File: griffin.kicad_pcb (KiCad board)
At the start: 2 copper layers, 150 x 100 mm, 41 parts, among them IC1 ME6211C33M5G-N, J1 USB_B_Micro, J2 Conn_02x03_Odd_Even, J3 Conn_01x04, J4 Conn_01x11, J5 Conn_01x04, J6 Conn_01x20, J7 Conn_01x20, J8 Conn_01x14, J9 Conn_01x08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

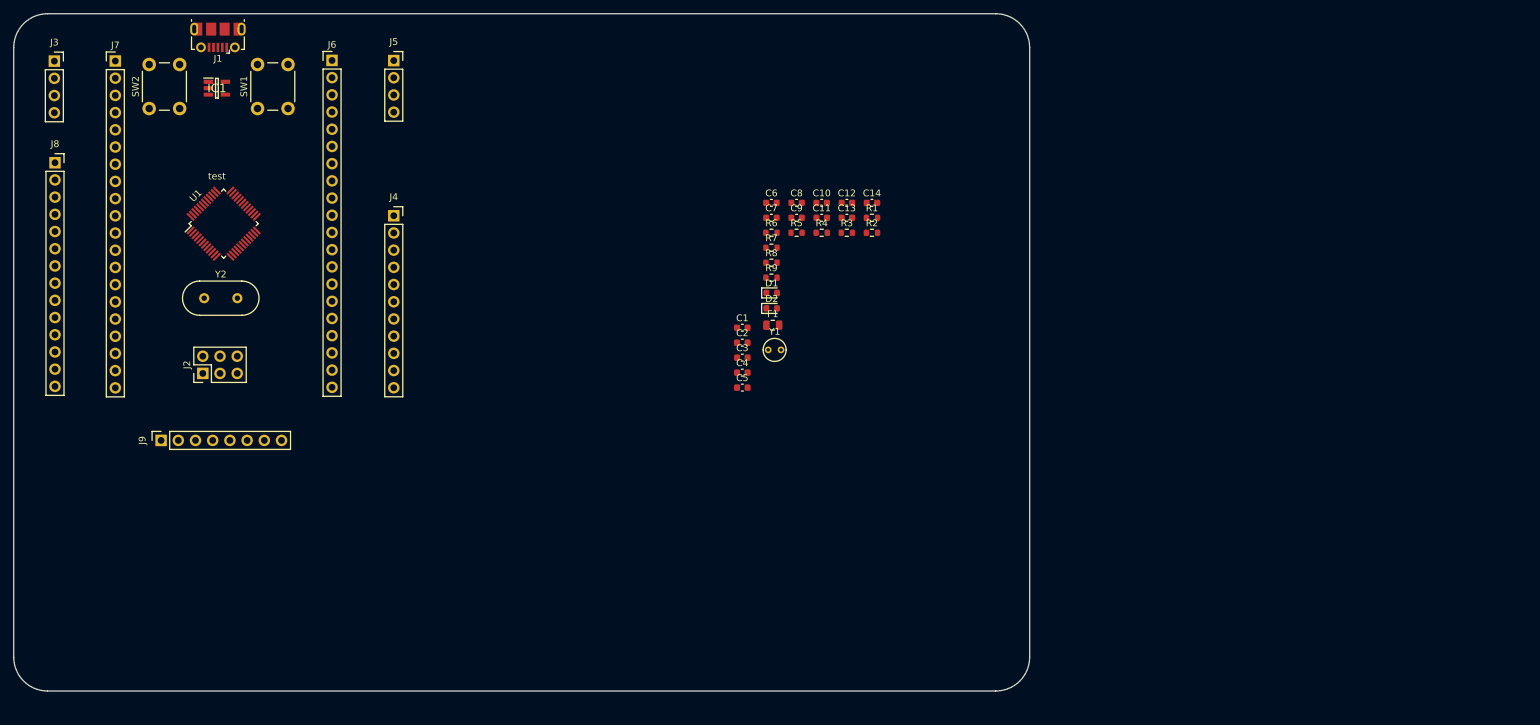
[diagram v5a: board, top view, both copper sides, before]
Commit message: support borad margin
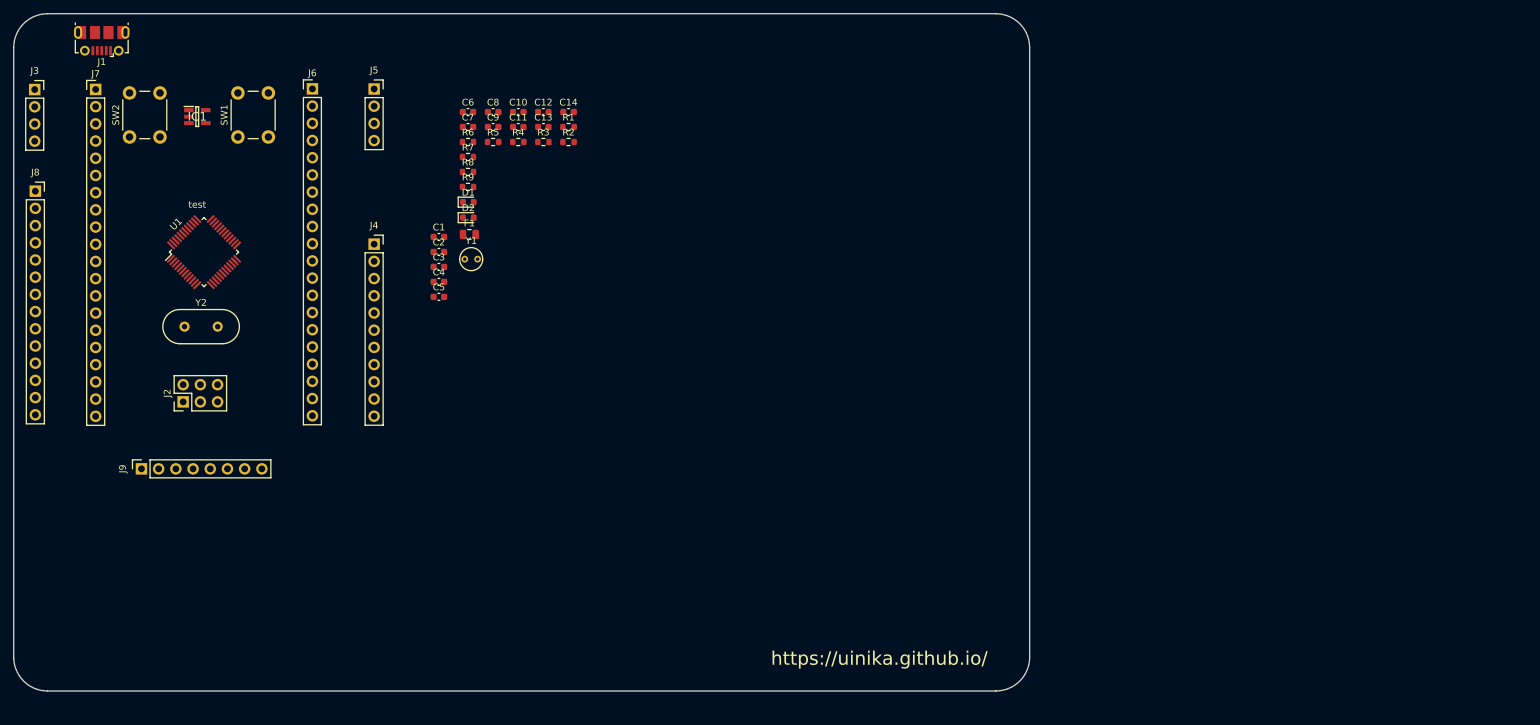
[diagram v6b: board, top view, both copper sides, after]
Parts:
- moved C1 46.8 mm to (104.8, 74.0)
- moved C2 46.8 mm to (104.8, 76.2)
- moved C3 46.8 mm to (104.8, 78.4)
- moved C4 46.8 mm to (104.8, 80.6)
- moved C5 46.8 mm to (104.8, 82.8)
- moved D1 46.8 mm to (109.1, 68.8)
- moved D2 46.8 mm to (109.1, 71.1)
- moved F1 46.8 mm to (109.3, 73.6)
- moved C10 46.8 mm to (116.5, 55.5)
- moved C11 46.8 mm to (116.5, 57.7)
- moved C12 46.8 mm to (120.2, 55.5)
- moved C13 46.8 mm to (120.2, 57.7)
- moved C14 46.8 mm to (123.9, 55.5)
- moved C6 46.8 mm to (109.1, 55.5)
- moved C7 46.8 mm to (109.1, 57.7)
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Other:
- board text added: "https://uinika.github.io/"

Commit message: update
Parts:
- added P1: USB_C_Plug, Connector_USB:USB_C_Receptacle_Amphenol_12401610E4-2A, F.Cu at (87.0, 113.9)
- added SW3: SW_Push, Button_Switch_THT:SW_PUSH-12mm, F.Cu at (62.3, 123.3)
- C11: value 104 -> 105
- Y1: footprint Crystal:Crystal_Round_D3.0mm_Vertical -> Crystal:Crystal_SMD_3215-2Pin_3.2x1.5mm
- moved J6 83.1 mm to (58.0, 130.3), turned to 180 degrees
- moved J7 78.1 mm to (53.6, 130.3), turned to 180 degrees
- moved SW1 66.2 mm to (105.4, 118.1), turned to 180 degrees
- moved J3 62.4 mm to (87.7, 97.9)
- moved SW2 61.0 mm to (98.9, 105.4), turned to 0 degrees
- moved C1 57.7 mm to (99.2, 131.4)
- moved C2 56.0 mm to (95.5, 131.4)
- moved J1 55.8 mm to (97.5, 81.1)
- moved U1 53.0 mm to (87.4, 126.2), turned to 135 degrees
- moved C14 48.3 mm to (83.1, 81.3)
- moved R1 48.3 mm to (83.1, 83.5)
- moved R2 48.3 mm to (83.1, 85.7)
- moved J5 47.3 mm to (83.4, 97.9)
- moved R3 46.5 mm to (83.1, 88.0)
- moved J8 45.3 mm to (79.1, 97.3)
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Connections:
- C1 pad 2: +3V3 -> /+3.3V
- C11 pad 2: +3V3 -> Net-(C11-Pad2)
- C12 pad 2: +3V3 -> Net-(C11-Pad2)
- C2 pad 2: +3V3 -> /+3.3V
- C5 pad 2: +3V3 -> /+3.3V
- C6 pad 2: +3V3 -> /+3.3V
- D1 pad 2: +3V3 -> /+3.3V
- D2 pad 2: +3V3 -> /+3.3V
- F1 pad 2: +5V -> /+5V
- IC1 pad 5: +3V3 -> Net-(C11-Pad2)
- J1 pad 1: +5V -> Net-(J1-Pad1)
- J2 pad 1: +3V3 -> /+3.3V
- J2 pad 2: +3V3 -> /+3.3V
- J3 pad 4: +3V3 -> /+3.3V
- J4 pad 1: +5V -> /+5V
- J5 pad 1: +3V3 -> /+3.3V
- J6 pad 2: +5V -> /+5V
- J6 pad 3: +3V3 -> /+3.3V
- J6 pad 6: /PA0 -> /KEY0
- J7 pad 1: +3V3 -> /+3.3V
- J7 pad 2: +5V -> /+5V
- J8 pad 1: +5V -> /+3.3V
- J9 pad 2: +3V3 -> /+3.3V
- R3 pad 1: +3V3 -> /+3.3V
- R9 pad 1: +3V3 -> /+3.3V
- SW2 pad 1: +3V3 -> /+3.3V
- U1 pad 10: /PA0 -> /KEY0
- U1 pad 24: +3V3 -> /+3.3V
- U1 pad 36: +3V3 -> /+3.3V
- U1 pad 48: +3V3 -> /+3.3V
- U1 pad 9: +3V3 -> /+3.3V
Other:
- board text removed: "test"

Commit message: update PCB
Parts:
- D1: value LED -> LED1; footprint LED_SMD:LED_0603_1608Metric -> LED_SMD:LED_0805_2012Metric
- D2: value LED -> LED2; footprint LED_SMD:LED_0603_1608Metric -> LED_SMD:LED_0805_2012Metric
- J5: footprint Connector_PinSocket_2.54mm:PinSocket_1x04_P2.54mm_Vertical -> Connector_PinHeader_2.54mm:PinHeader_1x04_P2.54mm_Vertical
- moved C1 71.8 mm to (85.8, 60.8), turned to 270 degrees
- moved C2 71.0 mm to (87.9, 60.8), turned to 270 degrees
- moved SW3 70.0 mm to (46.5, 55.2)
- moved P1 68.4 mm to (73.9, 46.7), turned to 180 degrees
- moved J9 55.9 mm to (65.5, 133.1)
- moved SW2 54.6 mm to (58.5, 68.6)
- moved SW1 53.3 mm to (85.1, 68.8), turned to 0 degrees
- moved J1 52.9 mm to (59.2, 44.6)
- moved C3 52.5 mm to (62.5, 110.3)
- moved R8 50.2 mm to (64.3, 123.7)
- moved J3 47.2 mm to (47.0, 74.0)
- moved C4 46.9 mm to (67.8, 110.3)
- moved R2 45.1 mm to (64.2, 126.8)
- moved J6 39.7 mm to (96.8, 122.0)
- moved R1 37.6 mm to (63.5, 115.6)
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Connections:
- net /+5V renamed +5V
- R7 pad 2: GND -> /LED2
